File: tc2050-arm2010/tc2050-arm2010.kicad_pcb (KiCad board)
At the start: 2 copper layers, 27.9 x 25.4 mm, 4 parts, among them J1 Conn_02x05_Odd_Even, J2 Conn_02x10_Odd_Even

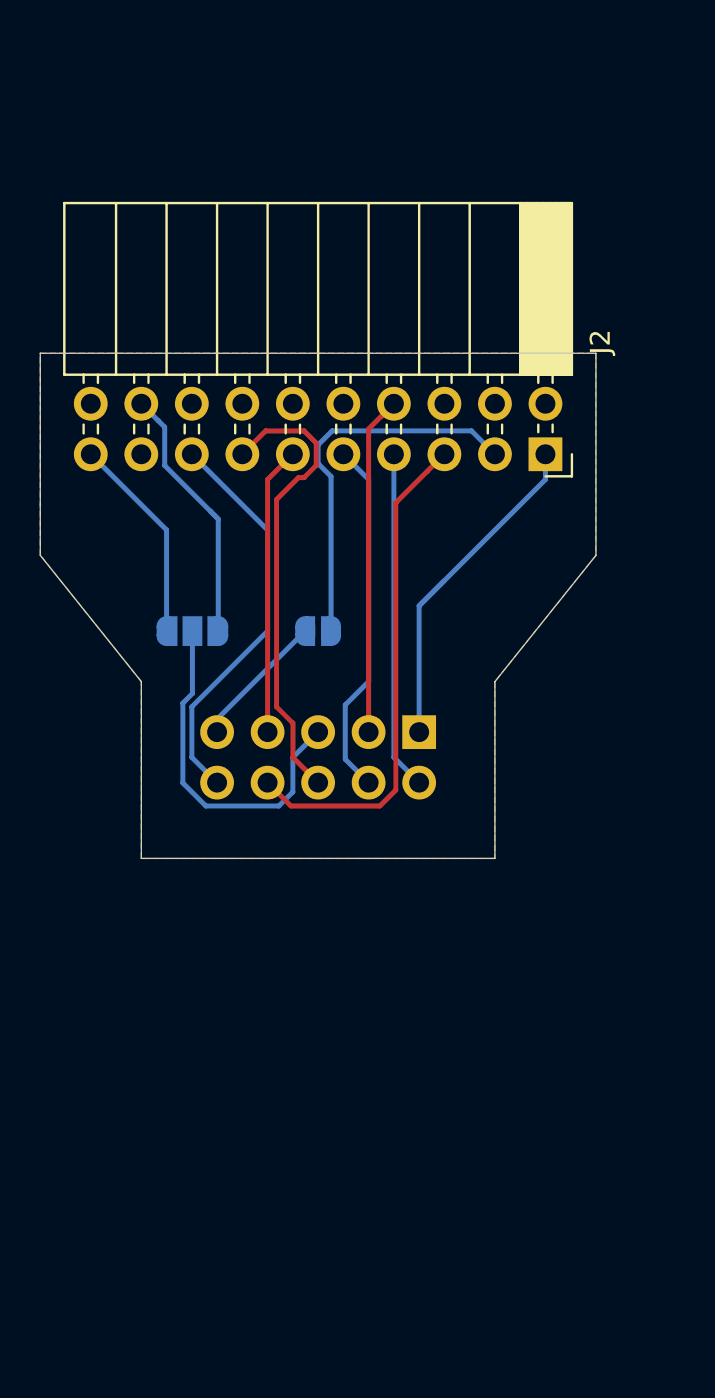
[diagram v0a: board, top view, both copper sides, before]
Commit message: New version also has TC2030 header as well as ARM10 and breakaway board from ARM10 to 7-pin SWD
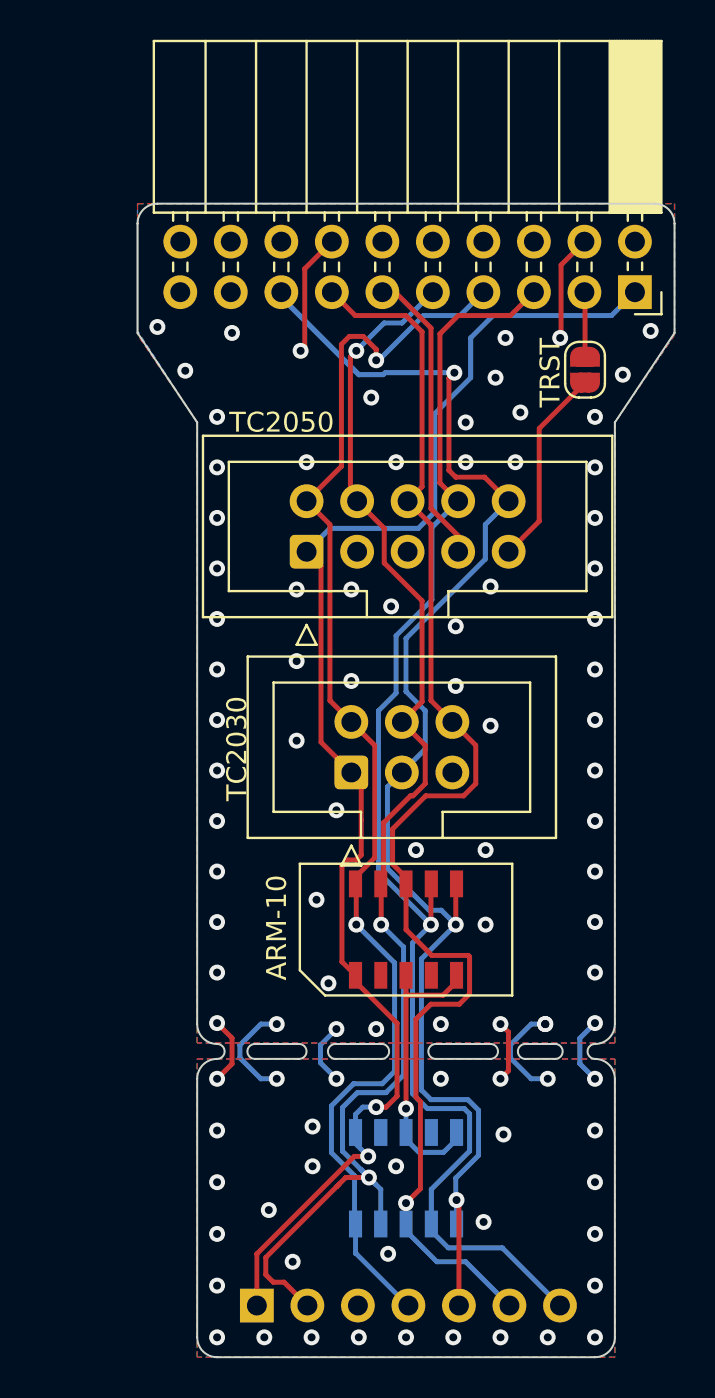
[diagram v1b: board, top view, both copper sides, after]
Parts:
- removed JP1: SolderJumper_3_Open, Jumper:SolderJumper-3_P1.3mm_Open_RoundedPad1.0x1.5mm
- added J3: Conn_ARM_JTAG_SWD_10, tc2050-arm2010:Samtec_MECF-05-02-NP-L-DV_2x05_P1.27mm_Socket_Horizontal, F.Cu at (178.4, 102.6)
- added J4: Conn_ARM_JTAG_SWD_10, tc2050-arm2010:Samtec_MECF-05-02-NP-L-DV_2x05_P1.27mm_Socket_Horizontal, B.Cu at (178.4, 115.1)
- added J5: Conn_02x03_Odd_Even, Connector_IDC:IDC-Header_2x03_P2.54mm_Vertical, F.Cu at (175.7, 94.7)
- added J6: Conn_01x07_Female, Connector_PinHeader_2.54mm:PinHeader_1x07_P2.54mm_Vertical, B.Cu at (170.9, 121.5)
- J1: footprint Connector_PinSocket_2.54mm:PinSocket_2x05_P2.54mm_Horizontal -> Connector_IDC:IDC-Header_2x05_P2.54mm_Vertical; moved to F.Cu
- JP2: moved to F.Cu
- moved JP2 18.8 mm to (187.4, 74.5), turned to -90 degrees
- moved J1 10.7 mm to (173.4, 83.6)
- moved J2 9.31 mm to (189.9, 70.6)
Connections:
- net /RESET renamed /nRESET
- net /SWCLK/TCLK renamed /SWCLK-TCLK
- net /SWDIO/TMS renamed /SWDIO-TMS
- net /SWO/TDO renamed /SWO-TDO
- J1 pad 5: Net-(J1-Pad5) -> GND
- J2 pad 19: +5V -> Net-(J2-Pad19)
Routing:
- net /nRESET: track 20.2 -> 77.3 mm, vias 0 -> 3
- net /VCC: track 18.4 -> 72.1 mm, vias 0 -> 2
- net /SWCLK-TCLK: track 18.0 -> 67.1 mm, vias 0 -> 3
- net /SWDIO-TMS: track 17.0 -> 65.2 mm, vias 0 -> 2
- net /SWO-TDO: track 23.4 -> 66.9 mm, vias 0 -> 1
- net /TDI: track 25.2 -> 67.4 mm, vias 0 -> 1
- net GND: track 30.5 -> 49.8 mm, vias 0 -> 98
- net Net-(J1-Pad5): track 17.7 -> 0.00 mm
- net /nTRST: track 19.3 -> 3.26 mm
- net +5V: track 10.5 -> 0.00 mm
- net Net-(J1-Pad9): track 6.91 -> 10.1 mm
- net /RTCK: track 14.5 -> 15.0 mm
- added copper zone on B.Cu, net GND
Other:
- board size 27.9 x 25.4 mm -> 27 x 58 mm
- net class Default removed
- board text added: "ARM-10"
- board text added: "CLK"
- board text added: "DIO"
- board text added: "SWO"
- board text added: "TC2030"
- board text added: "TC2050"
- board text added: "TDI"
- board text added: "VCC"
- board text added: "nRST"
- board text removed: "+5V"

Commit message: Trap for young players: gnd disconnected on host ARM10 when STM32 part cut off
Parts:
- added LOGO1: Logo_Open_Hardware_Small, Symbol:OSHW-Logo2_7.3x6mm_SilkScreen, B.Cu at (184.9, 76.1)
- added N1: Housing, Symbol:KiCad-Logo2_5mm_SilkScreen, B.Cu at (174.9, 75.6)
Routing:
- net GND: track 49.8 -> 44.0 mm, vias 98 -> 99
- net /VCC: track 72.1 -> 73.3 mm
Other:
- board text added: "JLCJLCJLCJLC"
- board text added: "itsonlyaudio.com"
- board text added: "nTRST"
- board text removed: "TRST"

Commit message: Latest exports for fabrication at JLCPCB and PCBWAY
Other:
- board text removed: "JLCJLCJLCJLC"
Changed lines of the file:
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@@
-    (effects (font (size 1 1) (thickness 0.15)))
-  )
-  (gr_text "JLCJLCJLCJLC" (at 178.41 102.64) (layer "F.SilkS")
     (effects (font (size 1 1) (thickness 0.15)))
   )
